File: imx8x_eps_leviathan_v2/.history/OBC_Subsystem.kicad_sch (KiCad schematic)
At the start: 32 parts, among them CN1 DF11-16DP-2DSA(08), U13 TPS1HB08BQPWPRQ1, U14 LT8612EUDE#PBF, U15 INA260AIPWR

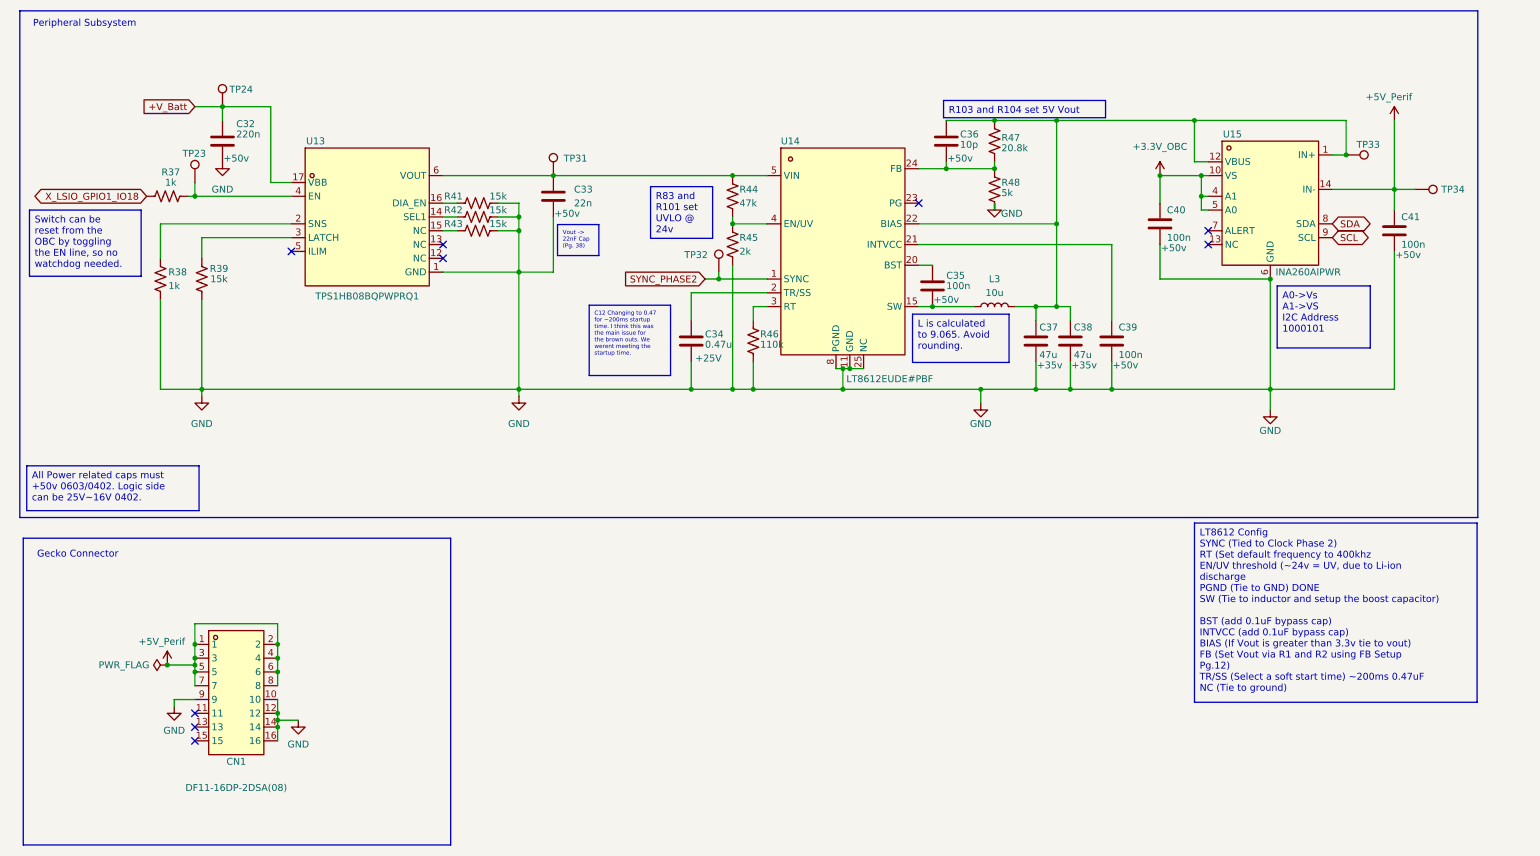
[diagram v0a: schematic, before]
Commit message: added R_Prot for CHA_GND
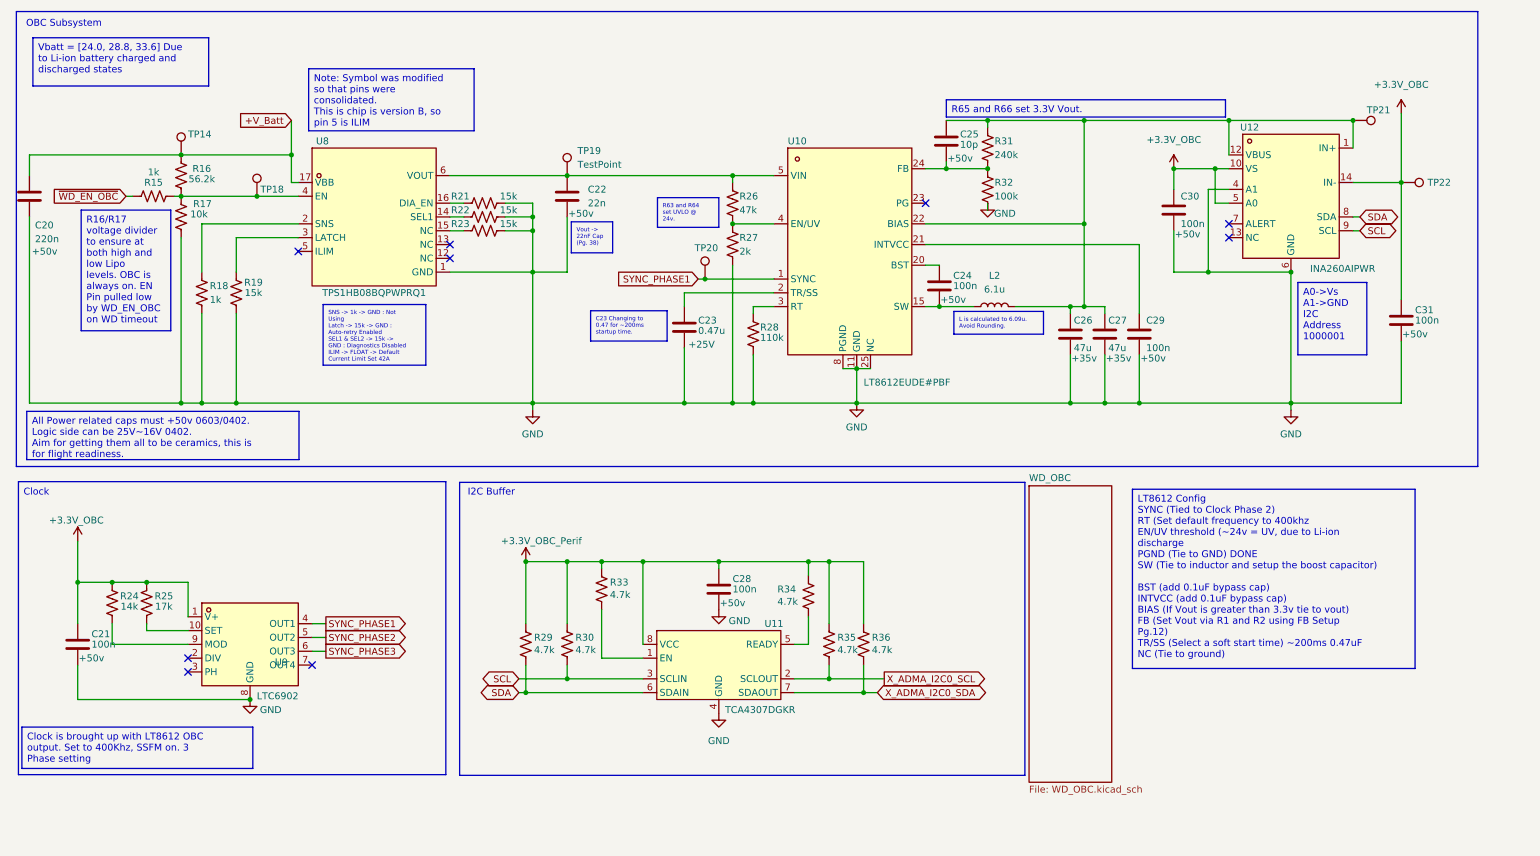
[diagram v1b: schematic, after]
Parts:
- removed C32: 220n, EPS:C0402, symbol Device:C
- removed C33: 22n, EPS:C0402, symbol Device:C
- removed C34: 0.47u, EPS:C0402, symbol Device:C
- removed C35, C39, C40, C41: 100n, EPS:C0402, symbol Device:C
- removed C36: 10p, EPS:C0402, symbol Device:C
- removed C37, C38: 47u, EPS:CAP-SMD_L7.3-W4.3-FD, symbol Device:C
- removed CN1: DF11-16DP-2DSA(08), EPS:CONN-TH_DF11-16DP-2DSA-08, symbol EPS:DF11-16DP-2DSA(08)
- removed L3: 10u, EPS:IND-SMD_L8.0-W8.0, symbol Device:L
- removed R37, R38: 1k, EPS:R0402, symbol Device:R_US
- removed R39, R41, R42, R43: 15k, EPS:R0402, symbol Device:R_US
- removed R44: 47k, EPS:R0402, symbol Device:R_US
- removed R45: 2k, EPS:R0402, symbol Device:R_US
- removed R46: 110k, EPS:R0402, symbol Device:R_US
- removed R47: 20.8k, EPS:R0402, symbol Device:R_US
- removed R48: 5k, EPS:R0402, symbol Device:R_US
- removed TP23, TP24, TP31, TP32, TP33, TP34: TestPoint, TestPoint:TestPoint_Pad_D1.0mm, symbol EPS:TestPoint
- removed U13: TPS1HB08BQPWPRQ1, EPS:HTSSOP-16_L5.0-W4.4-P0.65-LS6.4-TL-EP2.9, symbol EPS:TPS1HB08BQPWPRQ1
- removed U14: LT8612EUDE#PBF, EPS:QFN-28_L6.0-W3.0-P0.50-BL-EP, symbol EPS:LT8612EUDE#PBF
- removed U15: INA260AIPWR, EPS:TSSOP-16_L5.0-W4.4-P0.65-LS6.4-BL-1, symbol EPS:INA260AIPWR
- added C20: 220n, EPS:C0402, symbol Device:C
- added C21, C24, C28, C29, C30, C31: 100n, EPS:C0402, symbol Device:C
- added C22: 22n, EPS:C0402, symbol Device:C
- added C23: 0.47u, EPS:C0402, symbol Device:C
- added C25: 10p, EPS:C0402, symbol Device:C
- added C26, C27: 47u, EPS:CAP-SMD_L7.3-W4.3-FD, symbol Device:C
- added L2: 6.1u, EPS:IND-SMD_FTKB1207-6R1NT, symbol Device:L
- added R15, R18: 1k, EPS:R0402, symbol Device:R_US
- added R16: 56.2k, EPS:R0402, symbol Device:R_US
- added R17: 10k, EPS:R0402, symbol Device:R_US
- added R19, R21, R22, R23: 15k, EPS:R0402, symbol Device:R_US
- added R24: 14k, Resistor_SMD:R_0603_1608Metric, symbol Device:R_US
- added R25: 17k, Resistor_SMD:R_0603_1608Metric, symbol Device:R_US
- added R26: 47k, EPS:R0402, symbol Device:R_US
- added R27: 2k, EPS:R0402, symbol Device:R_US
- added R28: 110k, EPS:R0402, symbol Device:R_US
- added R29, R30, R33, R34, R35, R36: 4.7k, Resistor_SMD:R_0603_1608Metric, symbol Device:R_US
- added R31: 240k, EPS:R0402, symbol Device:R_US
- added R32: 100k, EPS:R0402, symbol Device:R_US
- added TP14, TP18, TP19, TP20, TP21, TP22: TestPoint, TestPoint:TestPoint_Pad_D1.0mm, symbol EPS:TestPoint
- added U10: LT8612EUDE#PBF, EPS:QFN-28_L6.0-W3.0-P0.50-BL-EP, symbol EPS:LT8612EUDE#PBF
- added U11: TCA4307DGKR, EPS:VSSOP-8_L3.0-W3.0-P0.65-LS4.9-BL, symbol EPS:TCA4307DGKR
- added U12: INA260AIPWR, EPS:TSSOP-16_L5.0-W4.4-P0.65-LS6.4-BL-1, symbol EPS:INA260AIPWR
- added U8: TPS1HB08BQPWPRQ1, EPS:HTSSOP-16_L5.0-W4.4-P0.65-LS6.4-TL-EP2.9, symbol EPS:TPS1HB08BQPWPRQ1
- added U9: LTC6902, EPS:MSOP-10_L3.0-W3.0-P0.50-LS5.0-BL, symbol EPS:LTC6902IMS#TRPBF
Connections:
- net +3.3V_OBC: now also C21.1, C30.1, C31.1, R24.1, R25.1, TP22.1, U12.10 (VS), U12.14 (IN-), U12.5 (A0), U9.1 (V+)
- net +V_Batt: now also C20.1, R16.2, TP14.1, U8.17 (VBB)
- net GND: now also C20.2, C21.2, C22.2, C23.2, C26.2, C27.2, C28.2, C29.2, C30.2, C31.2, R17.1, R18.1, R19.1, R21.2, R22.2, R23.2, R27.2, R28.2, R32.2, U10.11 (GND), U10.25 (NC), U10.8 (PGND), U11.4 (GND), U12.4 (A1), U12.6 (GND), U8.1 (GND), U9.8 (GND)
- net SCL: now also R30.2, U11.3 (SCLIN), U12.9 (SCL)
- net SDA: now also R29.2, U11.6 (SDAIN), U12.8 (SDA)
- net SYNC_PHASE2: now also U9.5 (OUT2)
- new net: C23.1, U10.2 (TR/SS)
- new net: C22.1, R26.1, TP19.1, U10.5 (VIN), U8.6 (VOUT)
- new net: R26.2, R27.1, U10.4 (EN/UV)
- new net: R33.2, U11.1 (EN)
- new net: R34.2, U11.5 (READY)
- new net: R21.1, U8.16 (DIA_EN)
- new net: C25.2, R31.2, R32.1, U10.24 (FB)
- new net: C25.1, C26.1, C27.1, L2.2, R31.1, TP21.1, U10.22 (BIAS), U12.1 (IN+), U12.12 (VBUS)
- new net: R23.1, U8.15 (NC)
- new net: R15.1, R16.1, R17.2, TP18.1, U8.4 (EN)
- new net: R22.1, U8.14 (SEL1)
- new net: R18.2, U8.2 (SNS)
- new net: R19.2, U8.3 (LATCH)
- new net: C24.1, U10.20 (BST)
- new net: C24.2, L2.1, U10.15 (SW)
- new net: R25.2, U9.10 (SET)
- new net: R24.2, U9.9 (MOD)
- new net: R28.1, U10.3 (RT)
- new net: C29.1, U10.21 (INTVCC)
- new net +3.3V_OBC_Perif: C28.1, R29.1, R30.1, R33.1, R34.1, R35.1, R36.1, U11.8 (VCC)
- new net SYNC_PHASE1: TP20.1, U10.1 (SYNC), U9.4 (OUT1)
- new net SYNC_PHASE3: U9.6 (OUT3)
- new net X_ADMA_I2C0_SCL: R35.2, U11.2 (SCLOUT)
- new net X_ADMA_I2C0_SDA: R36.2, U11.7 (SDAOUT)
- new net ~{WD_EN_OBC}: R15.2
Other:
- added sheet WD_OBC (WD_OBC.kicad_sch)
- note added: "Clock"
- note added: "I2C Buffer"
- note added: "OBC Subsystem"
- note removed: "Gecko Connector"
- note removed: "Peripheral Subsystem"

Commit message: Goodies
Updated USB to USB C. Added Diodes for USB. Improved Layout. Ready for some routing.
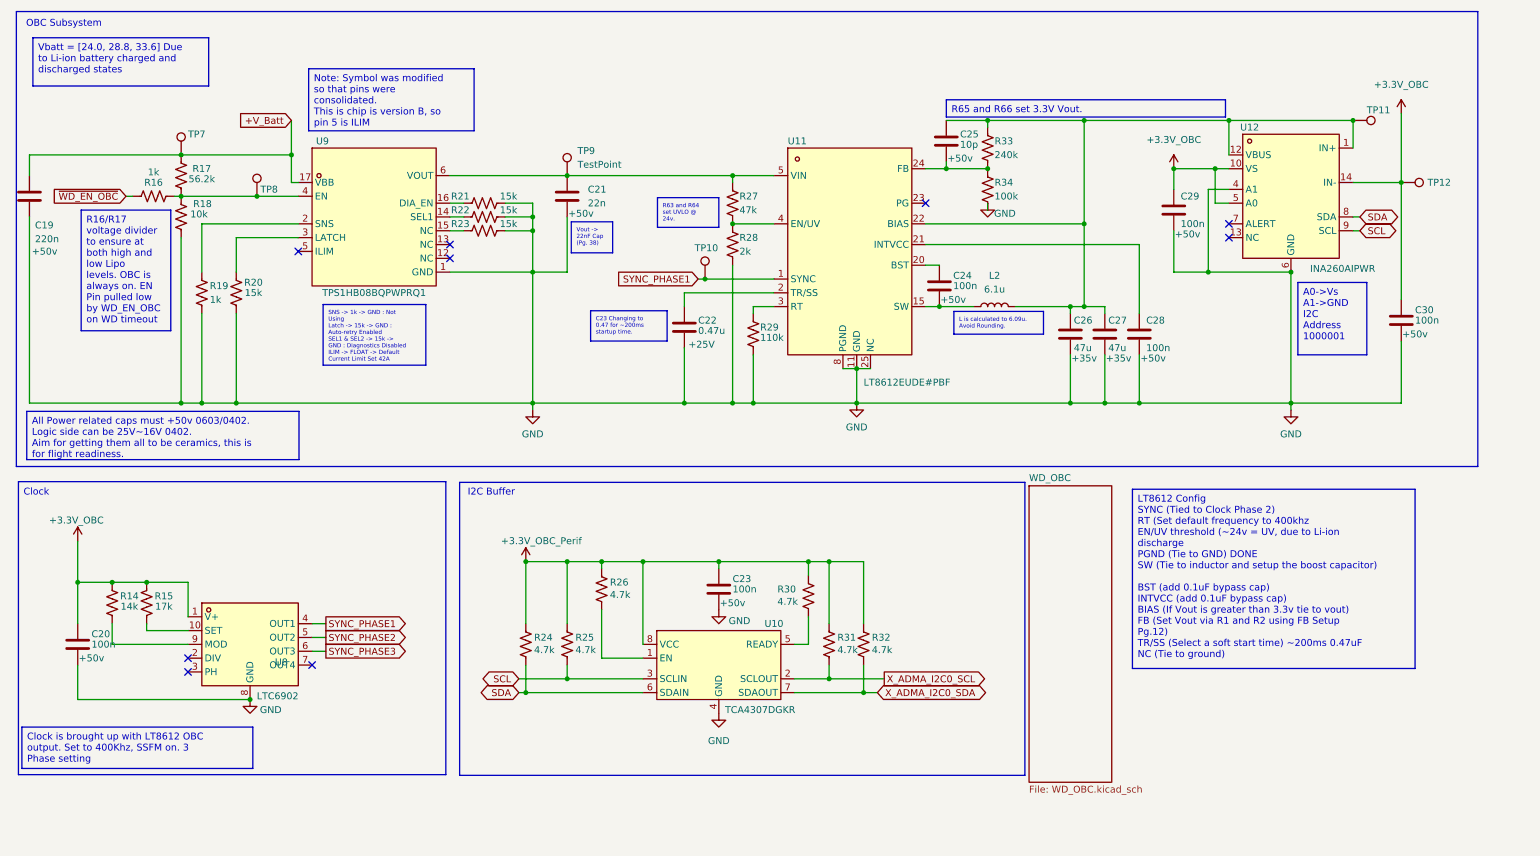
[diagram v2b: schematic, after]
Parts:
- renumbered C20 to C19, C21 to C20, C22 to C21, C23 to C22, C28 to C23, C29 to C28, C30 to C29, C31 to C30, R24 to R14, R25 to R15, R15 to R16, R16 to R17, R17 to R18, R18 to R19, R19 to R20, R29 to R24, R30 to R25, R33 to R26, R26 to R27, R27 to R28, R28 to R29, R34 to R30, R35 to R31, R36 to R32, R31 to R33, R32 to R34, TP20 to TP10, TP21 to TP11, TP22 to TP12, TP14 to TP7, TP18 to TP8, TP19 to TP9, U11 to U10, U10 to U11, U9 to U8, U8 to U9
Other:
- title: Leviathan V1 -> Leviathan V2
